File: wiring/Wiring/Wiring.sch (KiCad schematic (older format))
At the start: 12 parts, among them U1 MAIN, U2 E, U3 F, U4 G

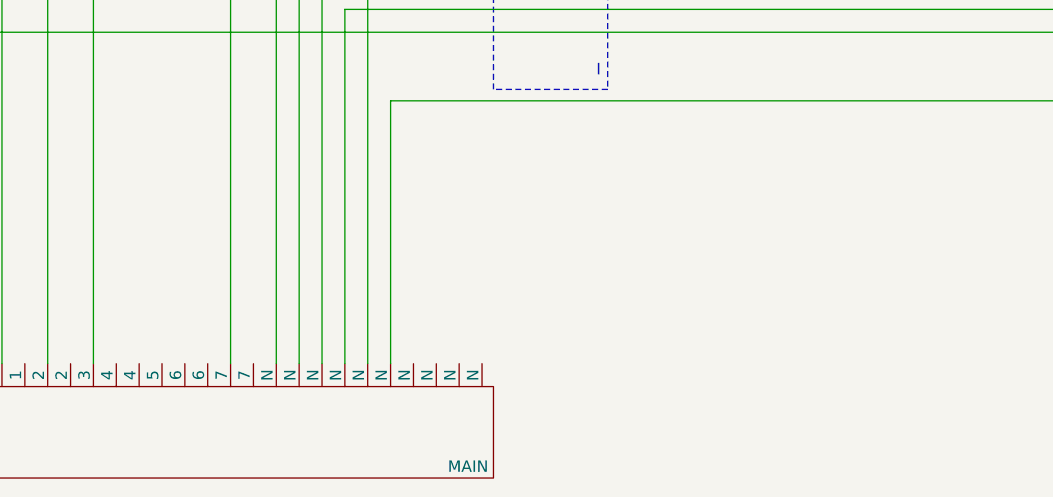
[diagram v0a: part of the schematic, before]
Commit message: Point out schematic bug: Router conn. to 5, not 1
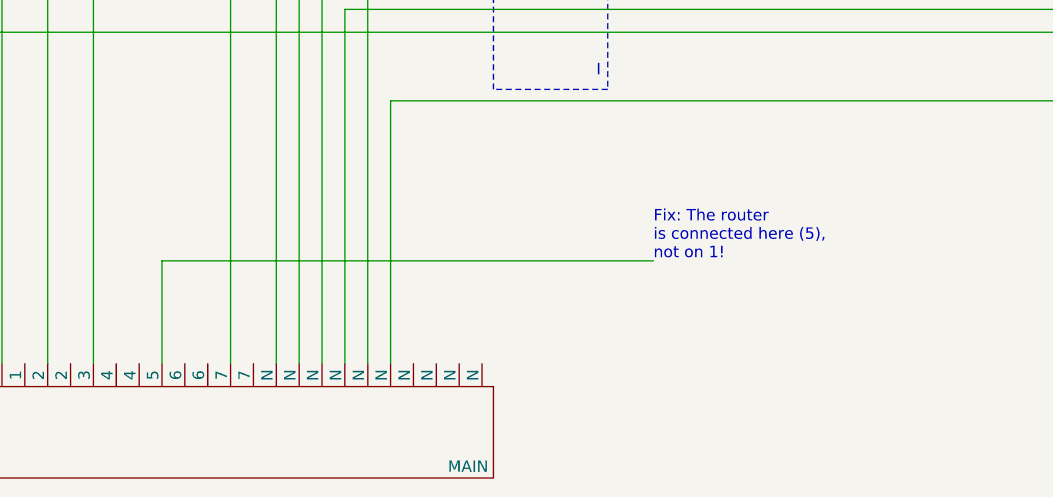
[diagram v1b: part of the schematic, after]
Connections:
- net at U3.~ (L): now also U?.10 (N); no longer U2.24 (L)
- net at U?.10 (N): no longer U3.~ (L)
- net at U2.~ (N): now also U?.12 (N); no longer U?.10 (N)
- net at U?.12 (N): no longer U2.~ (N)
- net at U1.~ (N): now also U?.16 (N)
- net at U?.12 (N): no longer U1.~ (N)
- net at U?.16 (N): no longer U1.~ (N)
- net at U?.~ (N): now also U?.12 (L) (x2)
- new net: U2.24 (L), U3.~ (L)
- new net: U2.14 (L), U?.12 (L)
- new net: U2.~ (N), U?.10 (N)
- new net: U1.~ (N), U?.12 (N)
- new net: U?.10 (N), U?.8 (N) (x2)
- new net: U?.12 (L), U?.9 (L) (x2)
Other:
- note added: "Fix: The router\nis connected here (5),\nnot on 1!"
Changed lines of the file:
@@
 	1    0    0    -1
 $EndComp
+Wire Wire Line
+	9800 11450 9800 11000
+Wire Wire Line
+	9800 11000 11950 11000
 Wire Bus Line
 	15750 6100 15950 6100
@@
 Wire Bus Line
 	11050 4600 11550 4600
+Text Notes 11950 11000 0    50   ~ 0
+Fix: The router\nis connected here (5),\nnot on 1!
 $EndSCHEMATC
